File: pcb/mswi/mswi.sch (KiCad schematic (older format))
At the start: 4 parts

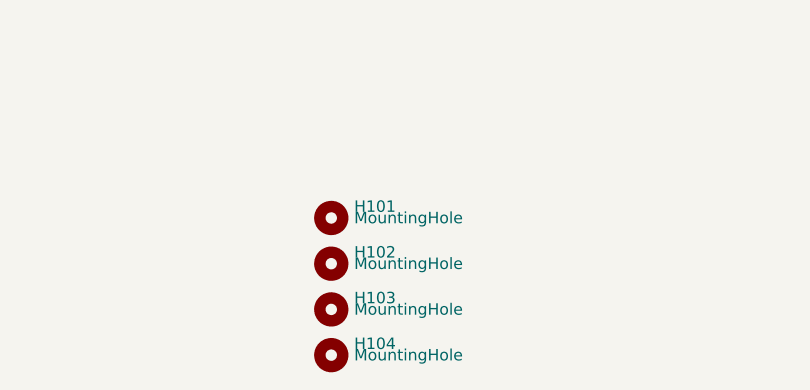
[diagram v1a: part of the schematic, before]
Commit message: screws removed
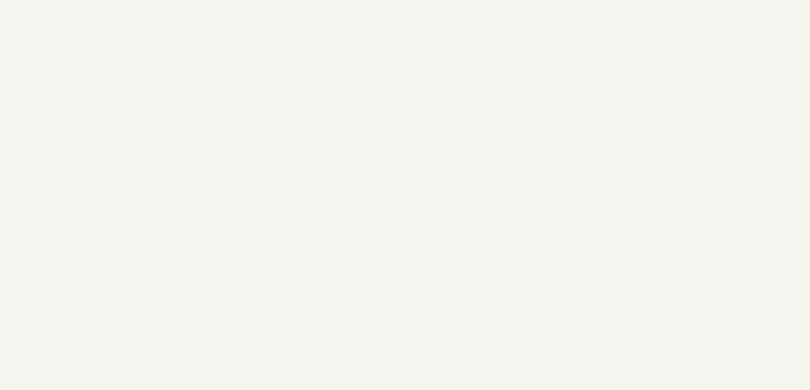
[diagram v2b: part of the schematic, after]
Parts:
- removed H101, H102, H103, H104: MountingHole, MountingHole:MountingHole_3.2mm_M3, symbol Mechanical:MountingHole
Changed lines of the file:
@@
 Wire Wire Line
 	6400 3550 5900 3550
-$Comp
-L Mechanical:MountingHole H104
-U 1 1 5BE9AF15
-P 5650 7000
-F 0 "H104" H 5750 7050 50  0000 L CNN
-F 1 "MountingHole" H 5750 7000 50  0000 L CNN
-F 2 "MountingHole:MountingHole_3.2mm_M3" H 5650 7000 50  0001 C CNN
-F 3 "~" H 5650 7000 50  0001 C CNN
-	1    5650 7000
-	1    0    0    -1
-$EndComp
-$Comp
-L Mechanical:MountingHole H103
-U 1 1 5BE9BC53
-P 5650 6800
-F 0 "H103" H 5750 6850 50  0000 L CNN
-F 1 "MountingHole" H 5750 6800 50  0000 L CNN
-F 2 "MountingHole:MountingHole_3.2mm_M3" H 5650 6800 50  0001 C CNN
-F 3 "~" H 5650 6800 50  0001 C CNN
-	1    5650 6800
-	1    0    0    -1
-$EndComp
-$Comp
-L Mechanical:MountingHole H102
-U 1 1 5BE9BC79
-P 5650 6600
-F 0 "H102" H 5750 6650 50  0000 L CNN
-F 1 "MountingHole" H 5750 6600 50  0000 L CNN
-F 2 "MountingHole:MountingHole_3.2mm_M3" H 5650 6600 50  0001 C CNN
-F 3 "~" H 5650 6600 50  0001 C CNN
-	1    5650 6600
-	1    0    0    -1
-$EndComp
-$Comp
-L Mechanical:MountingHole H101
-U 1 1 5BE9BC9F
-P 5650 6400
-F 0 "H101" H 5750 6450 50  0000 L CNN
-F 1 "MountingHole" H 5750 6400 50  0000 L CNN
-F 2 "MountingHole:MountingHole_3.2mm_M3" H 5650 6400 50  0001 C CNN
-F 3 "~" H 5650 6400 50  0001 C CNN
-	1    5650 6400
-	1    0    0    -1
-$EndComp
 Wire Wire Line
 	6500 3650 5900 3650
